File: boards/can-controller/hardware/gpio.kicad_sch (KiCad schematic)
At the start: 18 parts, among them J40 GPIO 1-4, J41 GPIO 5-8

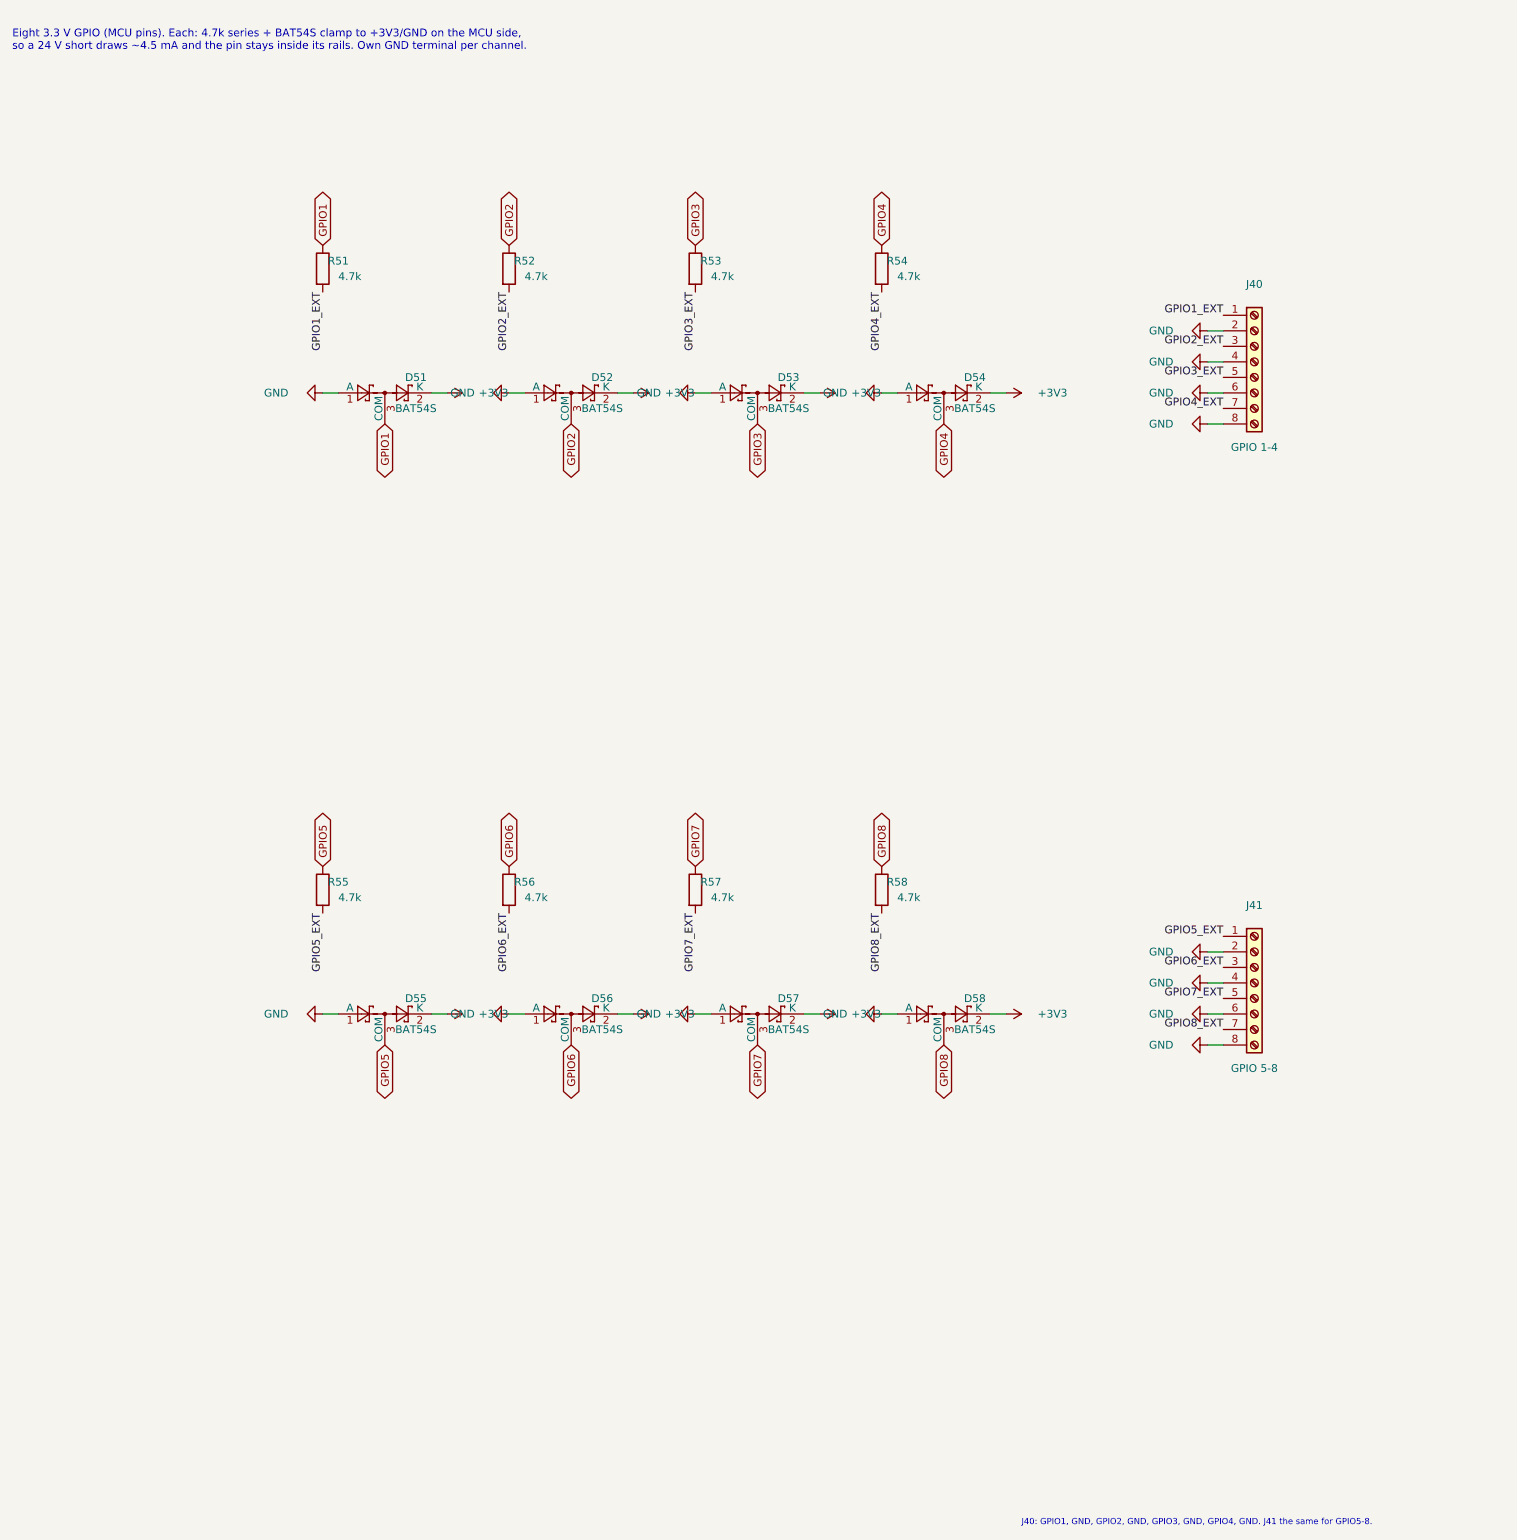
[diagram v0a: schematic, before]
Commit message: can-controller: double-level push-in terminals, re-placement, no DIN clips
- Phoenix SPTD 1,5 footprints (3-8 positions) generated from the Phoenix
  drawing (lib/footprint_src/Thl_Connector/phoenix_sptd.py)
- Schematic: J40 GPIO 2x8 (GPIO1-8 / GND), J50 ANALOG 2x6 (AI1-4, AO1-2 /
  GND), J30 RELAY 2x8 (OUT1-8 / +12 V); relay LEDs moved to the 12 V side
  (+12 V -> 4.7k -> LED -> OUTn); J41 removed
- Placement rev 2: GPIO and analog on the left edge, relay on the bottom;
  12 V block x > 140, y > 160 plus the CAN strip; all ISO1044 on x = 168;
  relay LEDs behind their terminal pins; CAN LEDs in a column
- DIN clip holes removed (3D-printed adapter on the M2.5 holes instead)
- DRC clean apart from unrouted nets and silkscreen

Co-Authored-By: Claude Opus 5.5 <noreply@anthropic.com>
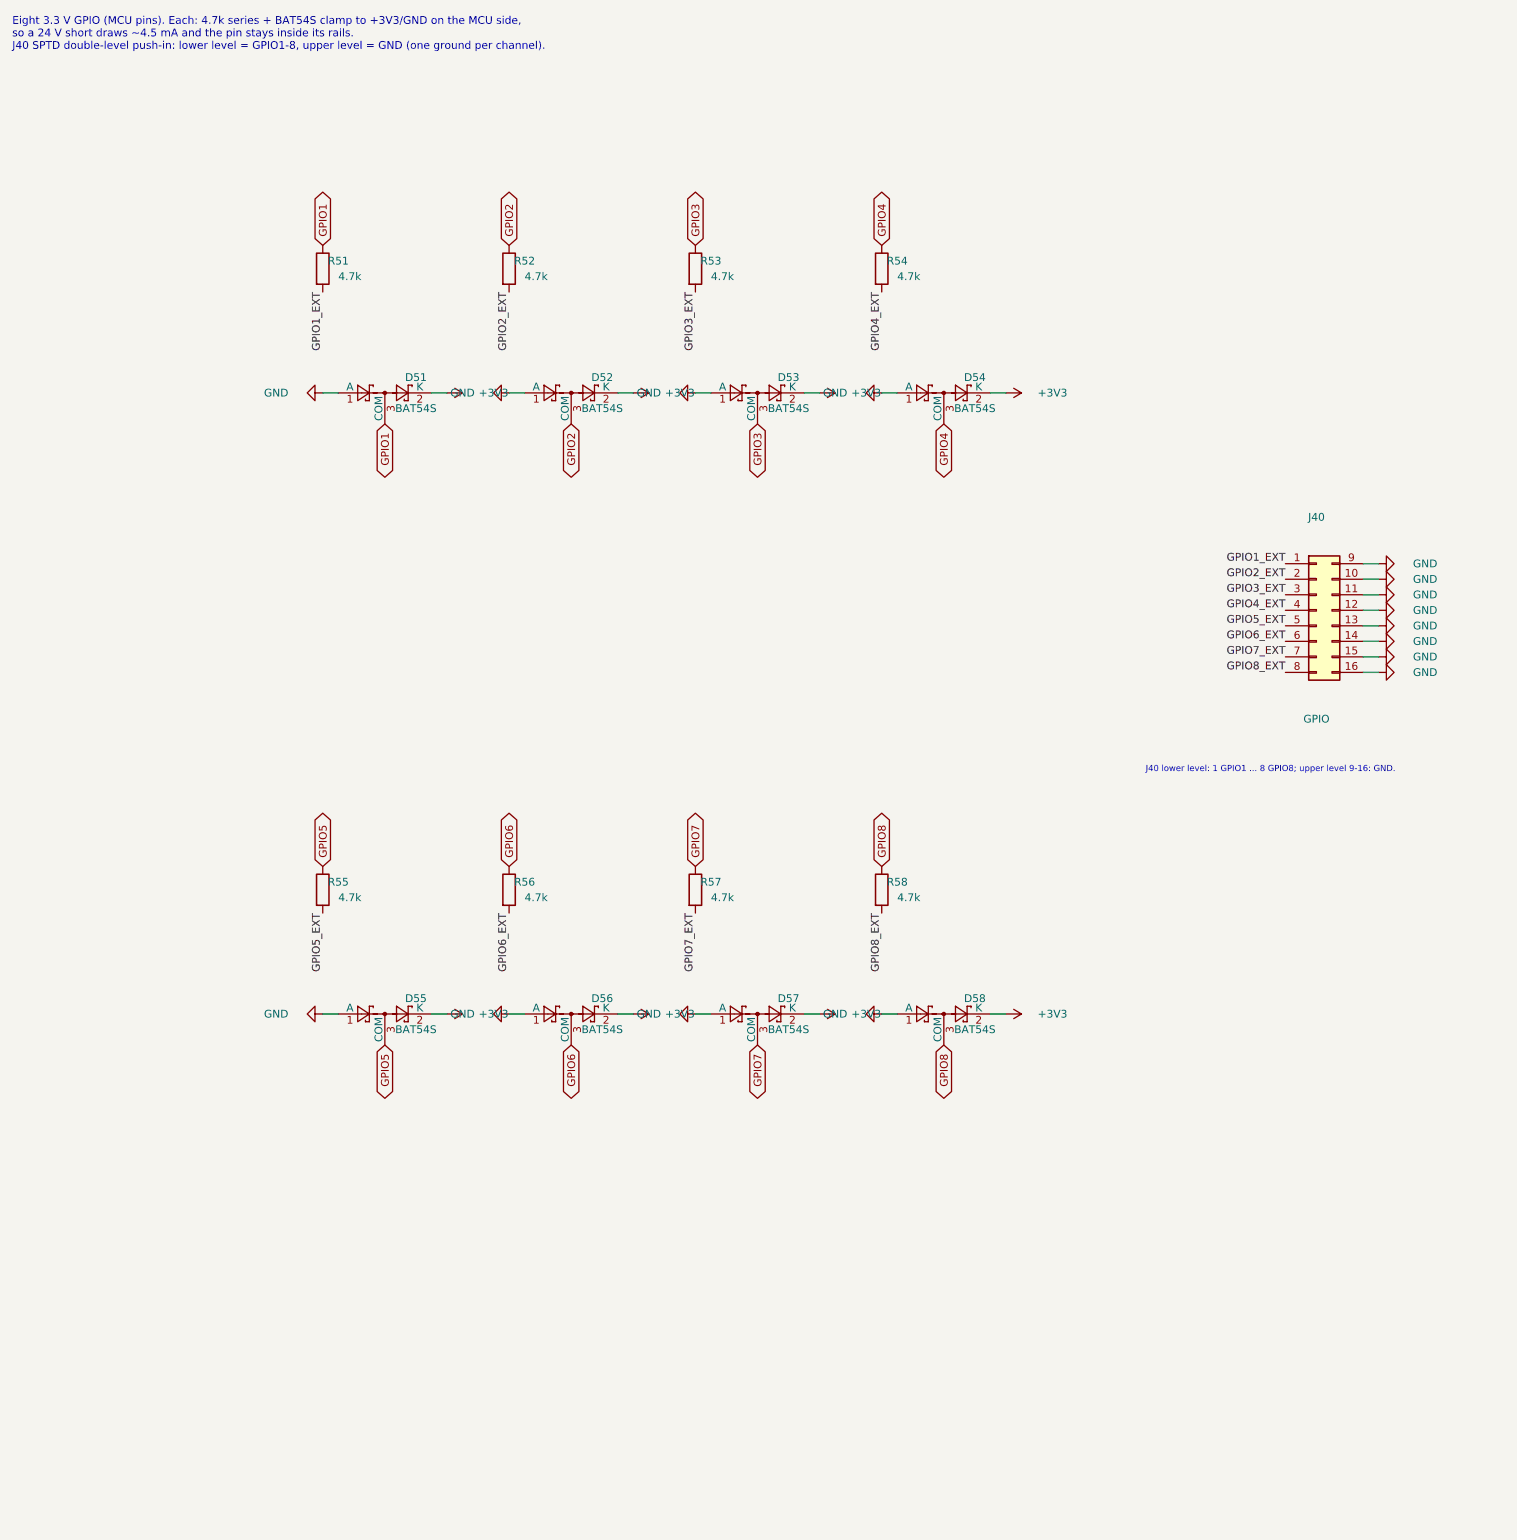
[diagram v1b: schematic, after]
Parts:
- removed J40: GPIO 1-4, Connector_Phoenix_MC:PhoenixContact_MC_1,5_8-G-3.5_1x08_P3.50mm_Horizontal, symbol Connector:Screw_Terminal_01x08
- removed J41: GPIO 5-8, Connector_Phoenix_MC:PhoenixContact_MC_1,5_8-G-3.5_1x08_P3.50mm_Horizontal, symbol Connector:Screw_Terminal_01x08
- added J40: GPIO, Thl_Connector:PhoenixContact_SPTD_1,5_8-H-3,5_2x08_P3.5mm_Horizontal, symbol Connector_Generic:Conn_02x08_Top_Bottom
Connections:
- net GND: now also J40.10 (Pin_10), J40.11 (Pin_11), J40.12 (Pin_12), J40.13 (Pin_13), J40.14 (Pin_14), J40.15 (Pin_15), J40.16 (Pin_16), J40.9 (Pin_9)
- net GPIO1_EXT: now also J40.1 (Pin_1)
- net GPIO2_EXT: now also J40.2 (Pin_2)
- net GPIO3_EXT: now also J40.3 (Pin_3)
- net GPIO4_EXT: now also J40.4 (Pin_4)
- net GPIO5_EXT: now also J40.5 (Pin_5)
- net GPIO6_EXT: now also J40.6 (Pin_6)
- net GPIO7_EXT: now also J40.7 (Pin_7)
- net GPIO8_EXT: now also J40.8 (Pin_8)
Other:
- note added: "Eight 3.3 V GPIO (MCU pins). Each: 4.7k series + BAT54S clamp to +3V3/GND on the MCU side, so a 24 V short draws ~4.5 mA and the pin stays inside its rails. J40 SPTD double-level push-in: lower level = GPIO1-8, upper level = GND (one ground per channel)."
- note added: "J40 lower level: 1 GPIO1 ... 8 GPIO8; upper level 9-16: GND."
- note removed: "Eight 3.3 V GPIO (MCU pins). Each: 4.7k series + BAT54S clamp to +3V3/GND on the MCU side, so a 24 V short draws ~4.5 mA and the pin stays inside its rails. Own GND terminal per channel."
- note removed: "J40: GPIO1, GND, GPIO2, GND, GPIO3, GND, GPIO4, GND. J41 the same for GPIO5-8."
